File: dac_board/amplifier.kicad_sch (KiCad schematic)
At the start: 29 parts

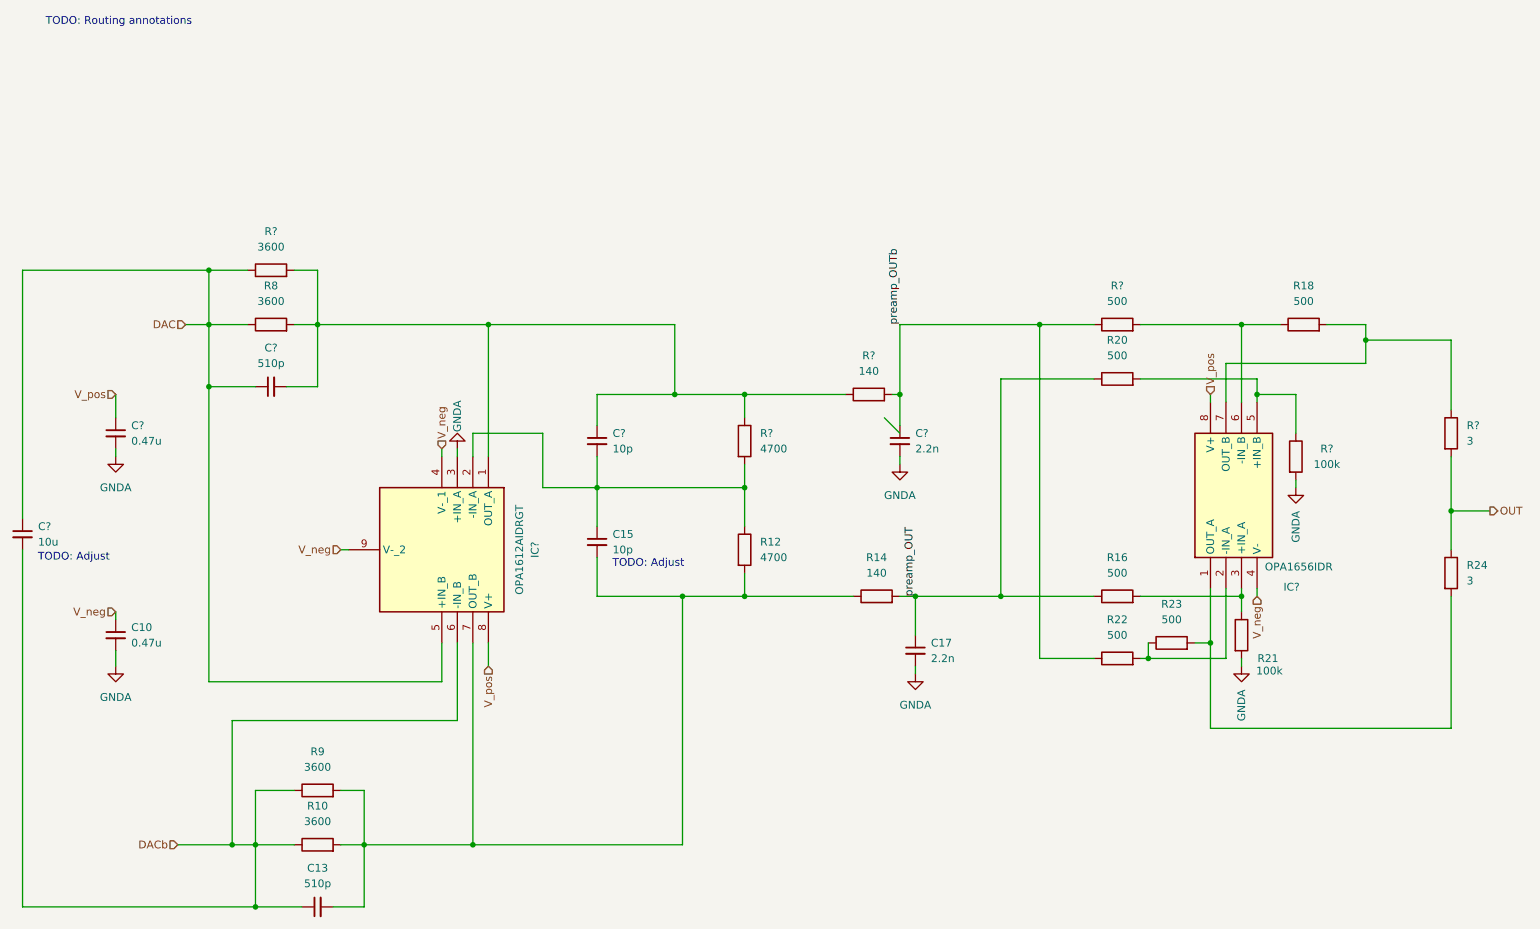
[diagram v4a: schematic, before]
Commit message: Added additional details to amplifier schematic
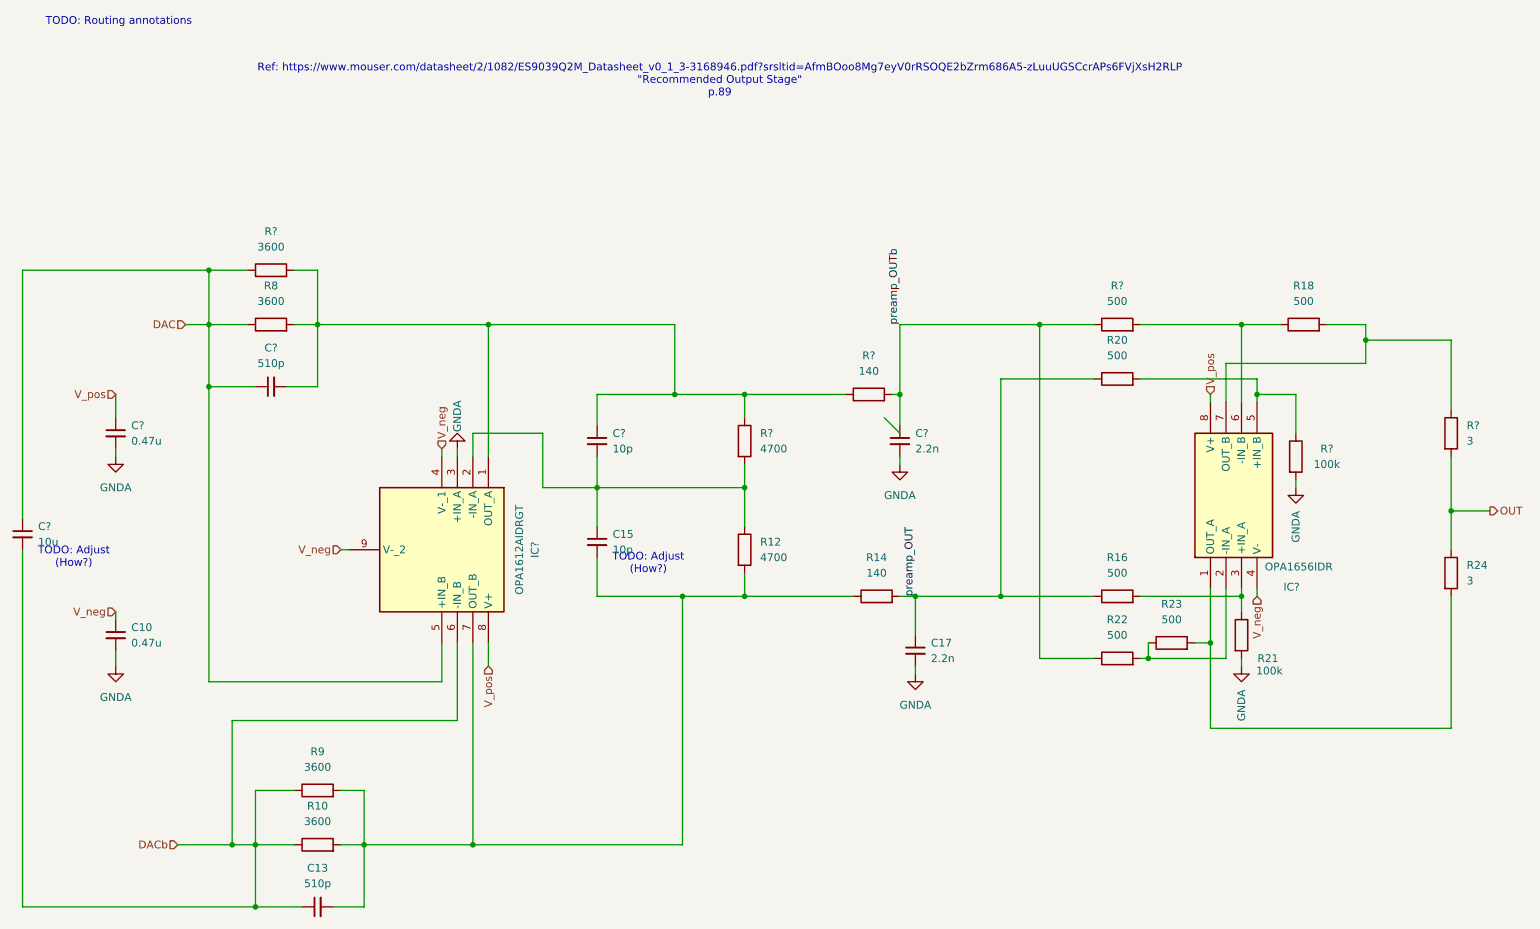
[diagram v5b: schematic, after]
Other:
- note added: "Ref: https://www.mouser.com/datasheet/2/1082/ES9039Q2M_Datasheet_v0_1_3-3168946.pdf?srsltid=AfmBOoo8Mg7eyV0rRSOQE2bZrm686A5-zLuuUGSCcrAPs6FVjXsH2RLPr "Recommended Output Stage"r p.89"
- note added: "TODO: Adjust (How?)"
- note removed: "TODO: Adjust"
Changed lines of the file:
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@@
 		(title "Amplifier")
 	)
-	(text "TODO: Adjust"
+	(text "TODO: Adjust\n(How?)"
 		(exclude_from_sim no)
 		(at 120.142 107.696 0)
@@
 		)
 	)
-	(text "TODO: Adjust"
+	(text "TODO: Adjust\n(How?)"
 		(exclude_from_sim no)
 		(at 26.162 106.68 0)
 		(effects
 			(font
+				(size 1.27 1.27)
+			)
+		)
+	)
+	(text "Ref: https://www.mouser.com/datasheet/2/1082/ES9039Q2M_Datasheet_v0_1_3-3168946.pdf?srsltid=AfmBOoo8Mg7eyV0rRSOQE2bZrm686A5-zLuuUGSCcrAPs6FVjXsH2RLP\r\n\"Recommended Output Stage\"\r\np.89"
+		(exclude_from_sim no)
+		(at 131.826 28.702 0)
+		(effects
+			(font

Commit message: Added TVS protection, USB CC handling, grounded MCU pins, impedance-matched HF traces, and increased output current capability per consultation with circuit-board-design.com
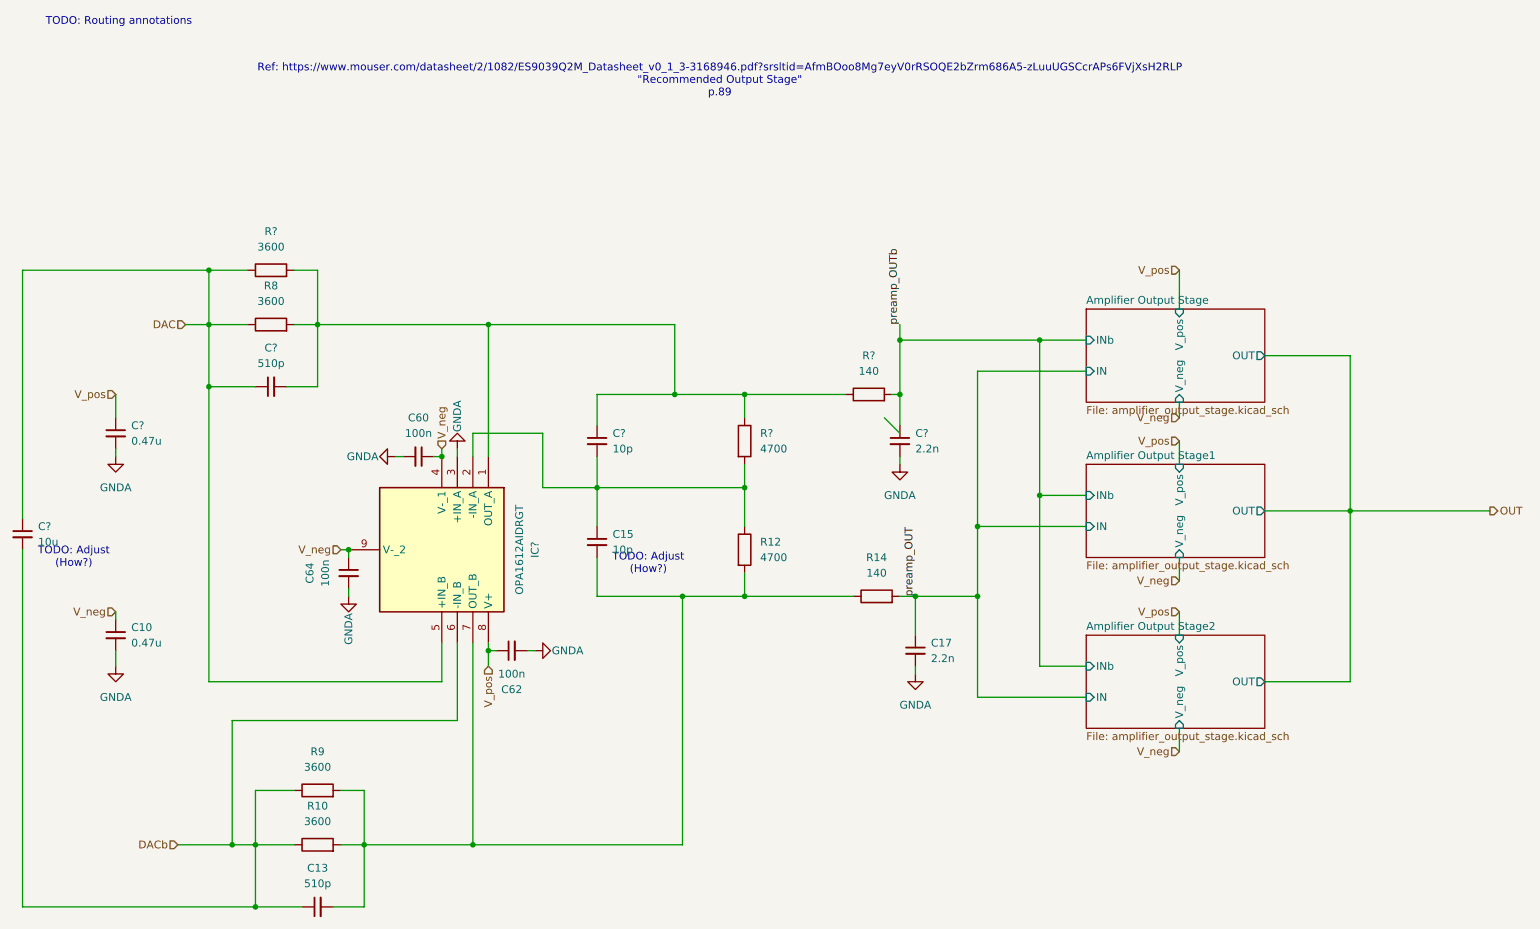
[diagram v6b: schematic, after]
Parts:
- removed IC?: OPA1656IDR, SOIC127P600X175-8N, symbol OPA1656IDR:OPA1656IDR
- removed R16, R18, R20, R22, R23, R?: 500, symbol Device:R
- removed R21, R?: 100k, symbol Device:R
- removed R24, R?: 3, symbol Device:R
- added C60, C62, C64: 100n, symbol Device:C_Small
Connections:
- net GNDA: now also C60.2, C62.2, C64.2
- net V_neg: now also C60.1, C64.1
- net V_pos: now also C62.1
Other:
- added sheet Amplifier Output Stage (amplifier_output_stage.kicad_sch)
- added sheet Amplifier Output Stage1 (amplifier_output_stage.kicad_sch)
- added sheet Amplifier Output Stage2 (amplifier_output_stage.kicad_sch)
